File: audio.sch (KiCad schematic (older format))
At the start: 37 parts

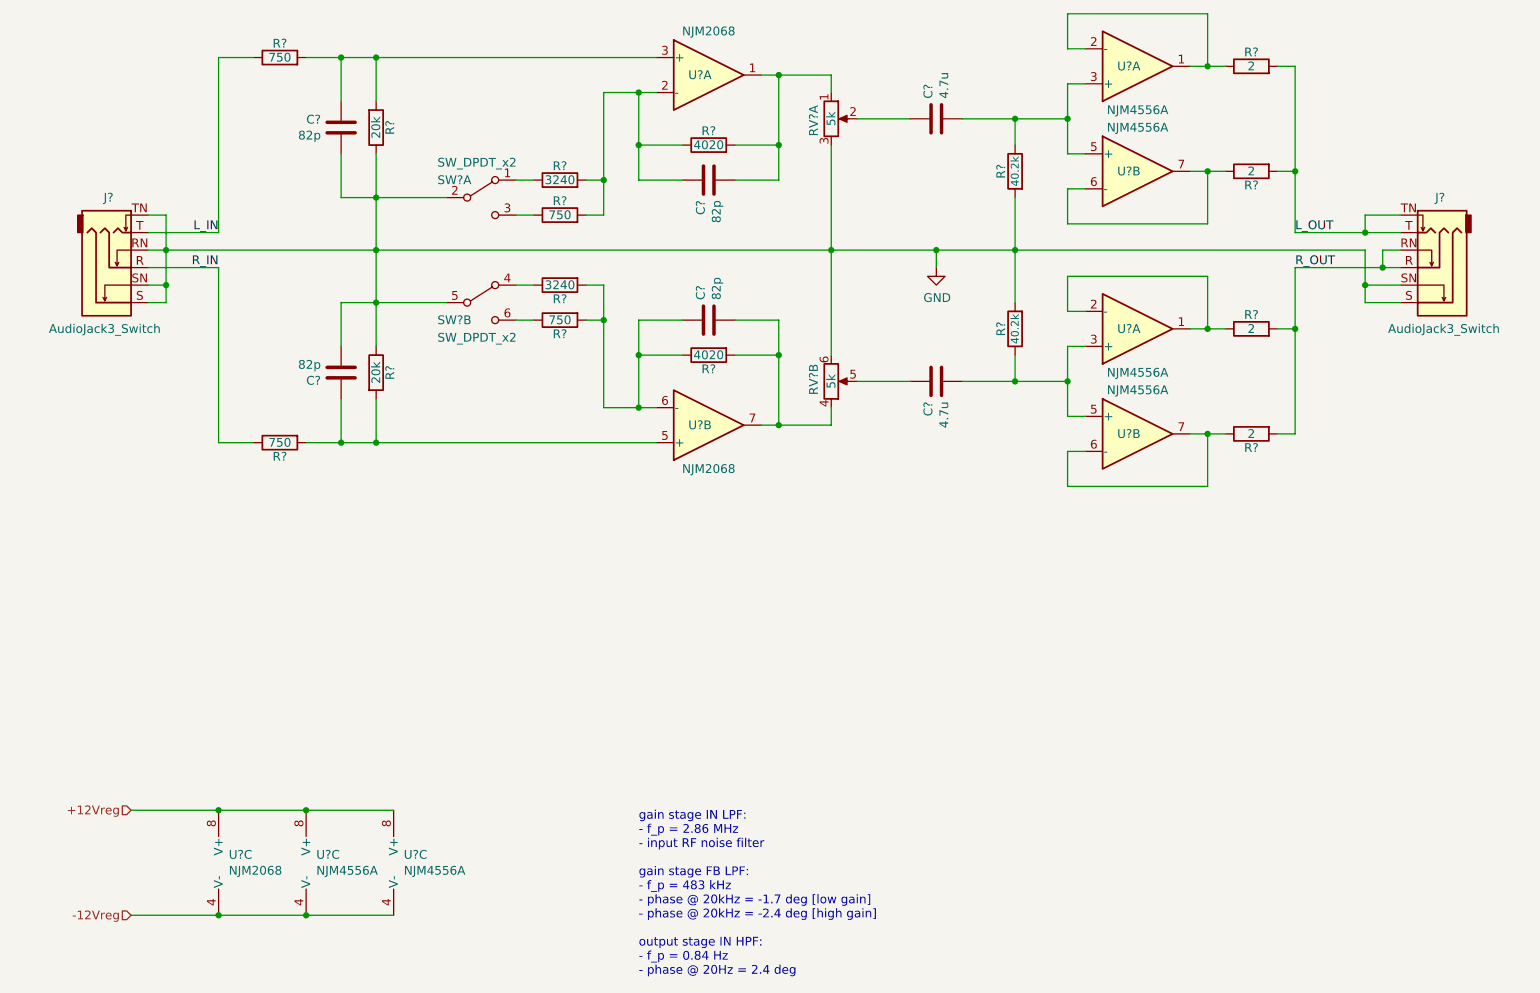
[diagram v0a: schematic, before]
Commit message: cleanup of wiring & notes in audio.sch
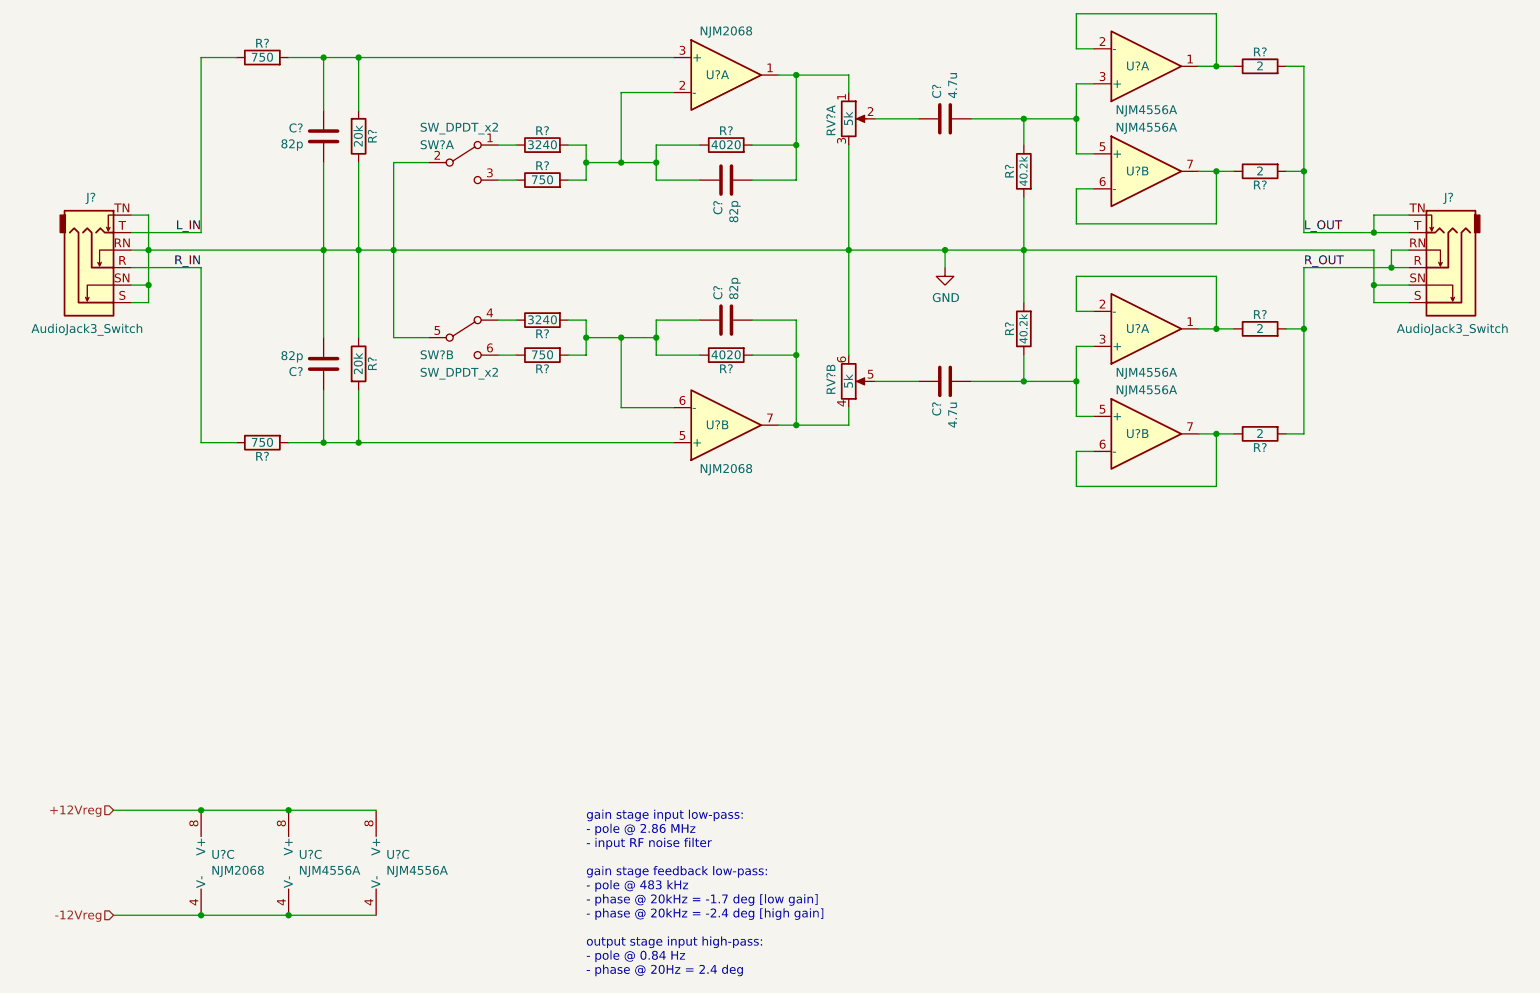
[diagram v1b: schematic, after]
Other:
- note added: "gain stage input low-pass:\n- pole @ 2.86 MHz\n- input RF noise filter\n\ngain stage feedback low-pass:\n- pole @ 483 kHz\n- phase @ 20kHz = -1.7 deg [low gain]\n- phase @ 20kHz = -2.4 deg [high gain]\n\noutput stage input high-pass:\n- pole @ 0.84 Hz\n- phase @ 20Hz = 2.4 deg"
- note removed: "gain stage IN LPF:\n- f_p = 2.86 MHz\n- input RF noise filter\n\ngain stage FB LPF:\n- f_p = 483 kHz\n- phase @ 20kHz = -1.7 deg [low gain]\n- phase @ 20kHz = -2.4 deg [high gain]\n\noutput stage IN HPF:\n- f_p = 0.84 Hz\n- phase @ 20Hz = 2.4 deg"
- moved on the sheet: C?, J?, R?, RV?A, RV?B, SW?A, SW?B, U?A, U?B, U?C

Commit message: add bourns SRU5028A inductor model & footprint
- switch location of bourns pot footprint
- update sourcing
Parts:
- RV?: footprint stdlibmods:Potentiometer_PTD902-1015K-A502 -> bourns:PTD902-1015K-A502
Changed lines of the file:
@@
 F 0 "RV?" V 6200 2550 50  0000 L CNN
 F 1 "5k" V 6300 2650 50  0000 C CNN
-F 2 "stdlibmods:Potentiometer_PTD902-1015K-A502" H 6300 2650 50  0001 C CNN
+F 2 "bourns:PTD902-1015K-A502" H 6300 2650 50  0001 C CNN
 F 3 "https://www.bourns.com/docs/product-datasheets/PTD90.pdf" H 6300 2650 50  0001 C CNN
 F 4 "Potentiometer 2 Gang Audio Taper 5kOhms" H 0   -600 50  0001 C CNN "Description"

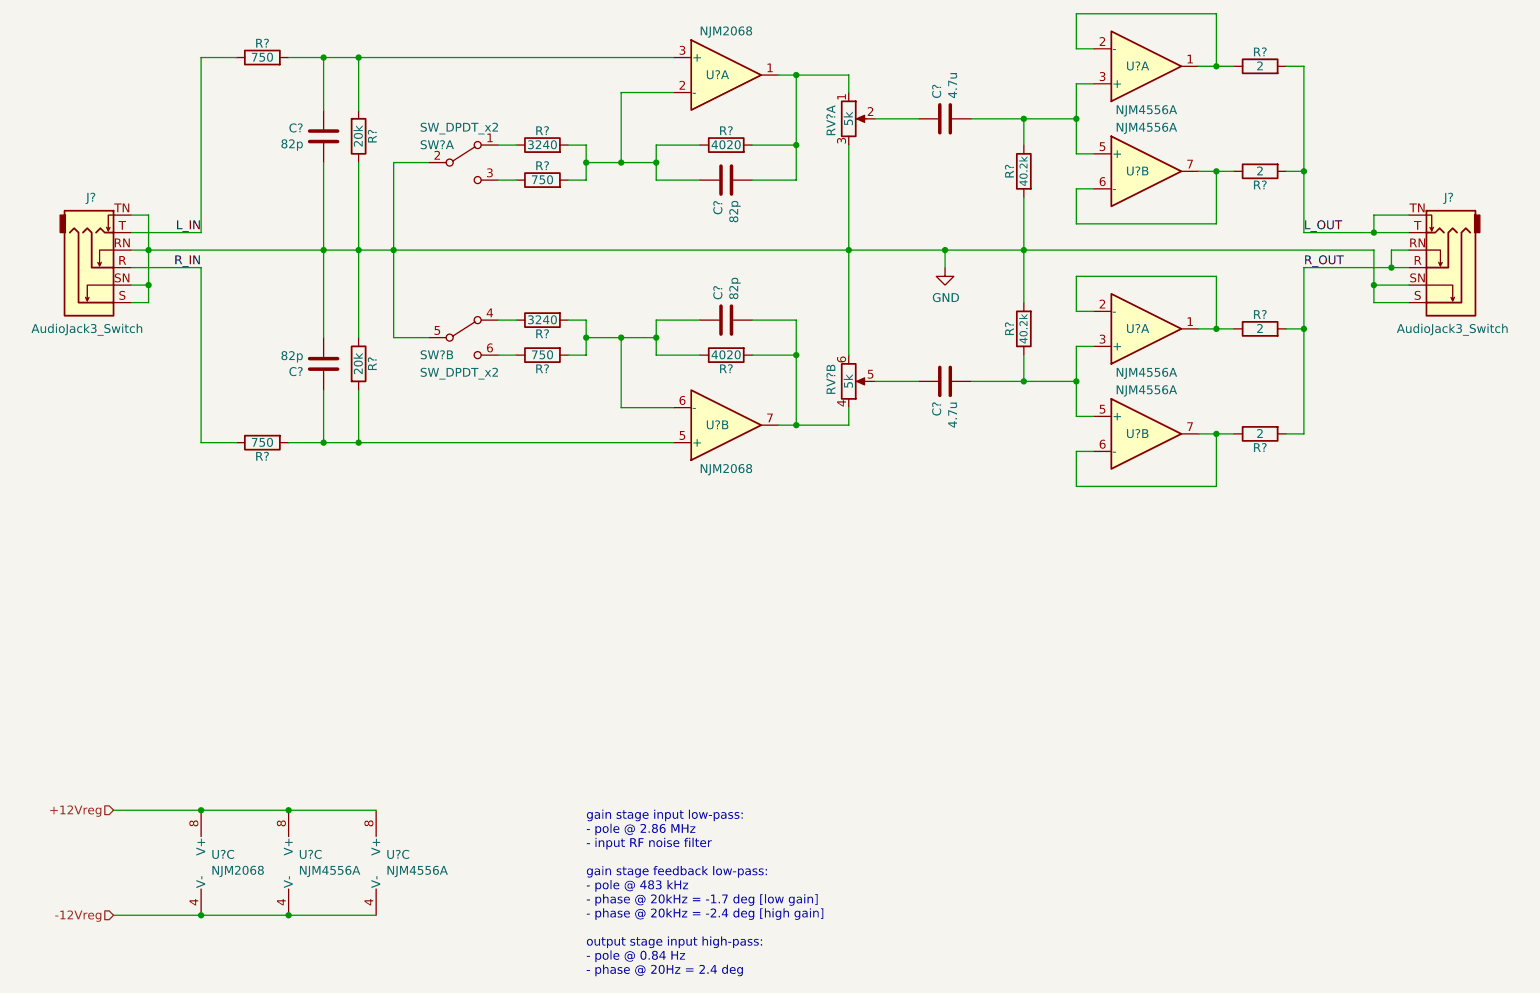
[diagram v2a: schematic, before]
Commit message: update output high pass filter
- replace WIMA 4.7uF coupling caps for KEMET 1uF
- replace 40.2k resistors with 274k
- update note
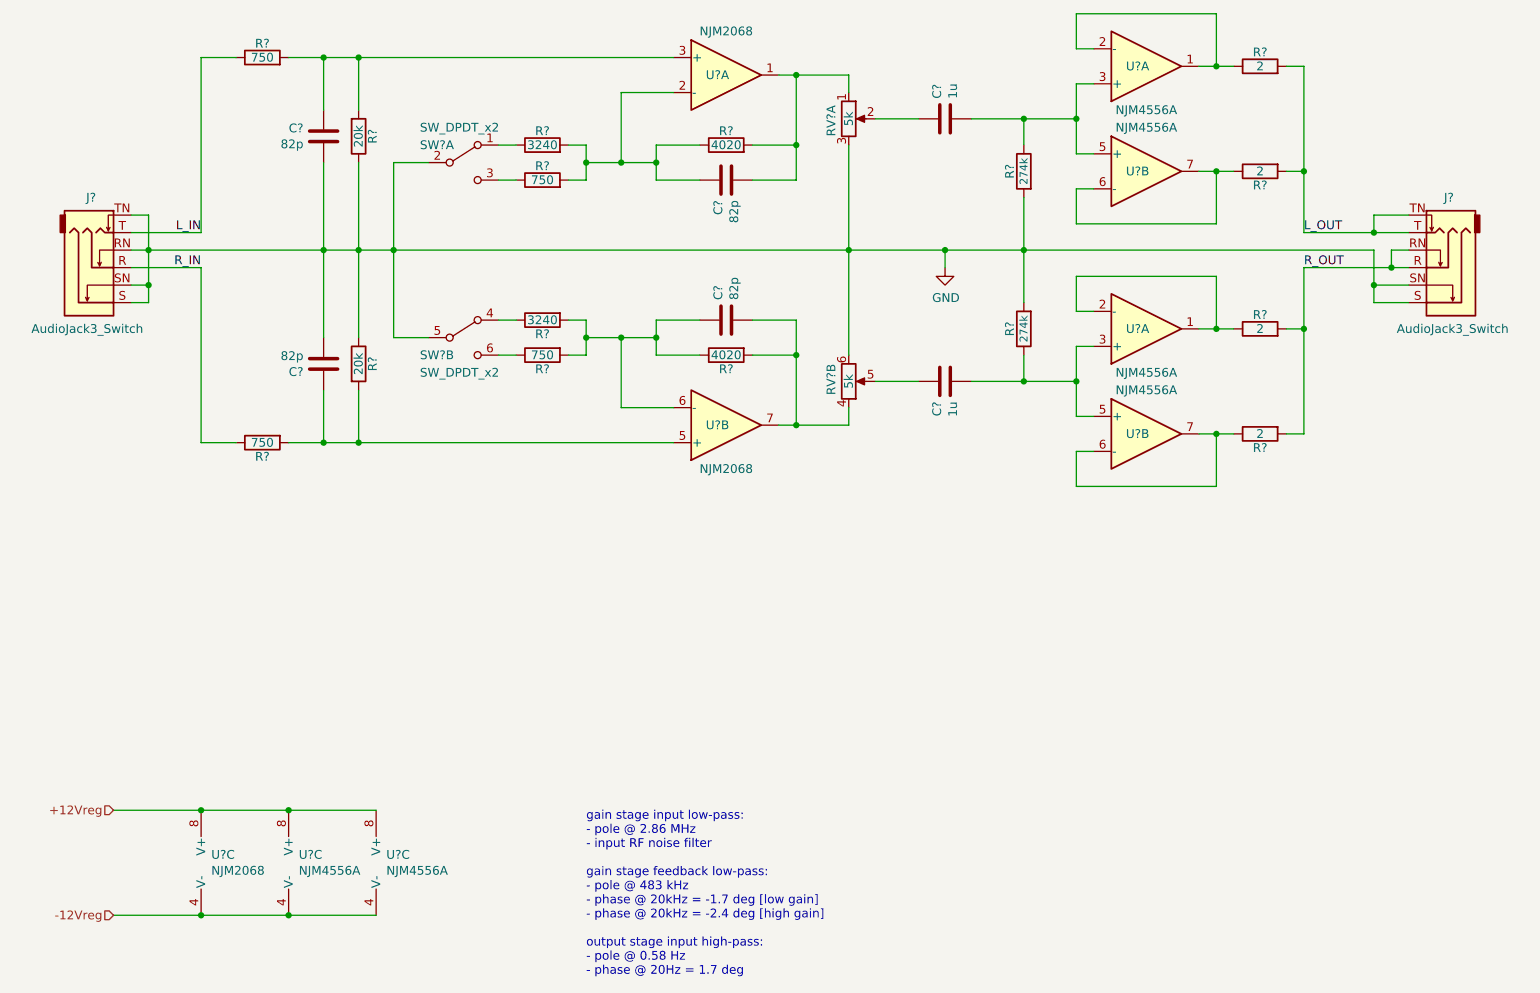
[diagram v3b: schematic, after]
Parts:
- C? (x2): value 4.7u -> 1u; footprint Capacitor_THT:C_Rect_L31.5mm_W15.0mm_P27.50mm_MKS4 -> (none); Description Film Capacitors 4.7uF 250 Volts 5% -> Film Capacitors 100V 1uF 5%; Manufacturer WIMA -> KEMET; Manufacturer Part Number MKP4F044706F00JSSD -> F612JT105J100R; Supplier Part Number 505-MKP4F044706F00JS -> 80-F612JT105J100R
- R? (x2): value 40.2k -> 274k; Description RES SMD 40.2K OHM 0.1% 1/8W 0805 Metal Film -> RES SMD 274K OHM 0.1% 1/8W 0805 Metal Film; Manufacturer Part Number ERA-6AEB4022V -> ERA-6AEB2743V; Supplier Part Number P40.2KDACT-ND -> P274KDACT-ND
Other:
- note added: "gain stage input low-pass:\n- pole @ 2.86 MHz\n- input RF noise filter\n\ngain stage feedback low-pass:\n- pole @ 483 kHz\n- phase @ 20kHz = -1.7 deg [low gain]\n- phase @ 20kHz = -2.4 deg [high gain]\n\noutput stage input high-pass:\n- pole @ 0.58 Hz\n- phase @ 20Hz = 1.7 deg"
- note removed: "gain stage input low-pass:\n- pole @ 2.86 MHz\n- input RF noise filter\n\ngain stage feedback low-pass:\n- pole @ 483 kHz\n- phase @ 20kHz = -1.7 deg [low gain]\n- phase @ 20kHz = -2.4 deg [high gain]\n\noutput stage input high-pass:\n- pole @ 0.84 Hz\n- phase @ 20Hz = 2.4 deg"
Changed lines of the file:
@@
 AR Path="/5CB56C16/5CEDA2A4" Ref="C?"  Part="1"
 F 0 "C?" H 6735 2604 50  0000 R CNN
-F 1 "4.7u" H 6735 2695 50  0000 R CNN
-F 2 "Capacitor_THT:C_Rect_L31.5mm_W15.0mm_P27.50mm_MKS4" H 6888 2500 50  0001 C CNN
-F 3 "https://www.mouser.com/datasheet/2/440/e_WIMA_MKP_4-1139861.pdf" H 6850 2650 50  0001 C CNN
-F 4 "Film Capacitors 4.7uF 250 Volts 5%" H 4400 -2500 50  0001 C CNN "Description"
-F 5 "WIMA" H 4400 -2500 50  0001 C CNN "Manufacturer"
-F 6 "MKP4F044706F00JSSD" H 4400 -2500 50  0001 C CNN "Manufacturer Part Number"
+F 1 "1u" H 6735 2695 50  0000 R CNN
+F 2 "" H 6888 2500 50  0001 C CNN
+F 3 "https://www.mouser.com/datasheet/2/212/KEM_F3065_F611_F612-1103659.pdf" H 6850 2650 50  0001 C CNN
+F 4 "Film Capacitors 100V 1uF 5%" H 4400 -2500 50  0001 C CNN "Description"
+F 5 "KEMET" H 4400 -2500 50  0001 C CNN "Manufacturer"
+F 6 "F612JT105J100R" H 4400 -2500 50  0001 C CNN "Manufacturer Part Number"
 F 7 "Mouser" H 4400 -2500 50  0001 C CNN "Supplier"
-F 8 "505-MKP4F044706F00JS" H 4400 -2500 50  0001 C CNN "Supplier Part Number"
+F 8 "80-F612JT105J100R" H 4400 -2500 50  0001 C CNN "Supplier Part Number"
 	1    6850 2650
 	0    1    1    0
@@
 AR Path="/5CB56C16/5CEDAB07" Ref="R?"  Part="1"
 F 0 "R?" V 7380 2950 50  0000 C CNN
-F 1 "40.2k" V 7300 2950 45  0000 C CNN
+F 1 "274k" V 7300 2950 45  0000 C CNN
 F 2 "Resistor_SMD:R_0805_2012Metric_Pad1.15x1.40mm_HandSolder" V 7230 2950 50  0001 C CNN
 F 3 "https://industrial.panasonic.com/cdbs/www-data/pdf/RDM0000/AOA0000C307.pdf" H 7300 2950 50  0001 C CNN
-F 4 "RES SMD 40.2K OHM 0.1% 1/8W 0805 Metal Film" H 7300 2950 50  0001 C CNN "Description"
+F 4 "RES SMD 274K OHM 0.1% 1/8W 0805 Metal Film" H 7300 2950 50  0001 C CNN "Description"
 F 5 "Panasonic Electronic Components" H 7300 2950 50  0001 C CNN "Manufacturer"
-F 6 "ERA-6AEB4022V" H 7300 2950 50  0001 C CNN "Manufacturer Part Number"
+F 6 "ERA-6AEB2743V" H 7300 2950 50  0001 C CNN "Manufacturer Part Number"
 F 7 "Digi-Key" H 7300 2950 50  0001 C CNN "Supplier"
-F 8 "P40.2KDACT-ND" H 7300 2950 50  0001 C CNN "Supplier Part Number"
+F 8 "P274KDACT-ND" H 7300 2950 50  0001 C CNN "Supplier Part Number"
 	1    7300 2950
 	-1   0    0    -1
@@
 AR Path="/5CB56C16/5CEE5E0B" Ref="C?"  Part="1"
 F 0 "C?" H 6735 4104 50  0000 R CNN
-F 1 "4.7u" H 6735 4195 50  0000 R CNN
-F 2 "Capacitor_THT:C_Rect_L31.5mm_W15.0mm_P27.50mm_MKS4" H 6888 4000 50  0001 C CNN
-F 3 "https://www.mouser.com/datasheet/2/440/e_WIMA_MKP_4-1139861.pdf" H 6850 4150 50  0001 C CNN
-F 4 "Film Capacitors 4.7uF 250 Volts 5%" H 4400 -1000 50  0001 C CNN "Description"
-F 5 "WIMA" H 4400 -1000 50  0001 C CNN "Manufacturer"
-F 6 "MKP4F044706F00JSSD" H 4400 -1000 50  0001 C CNN "Manufacturer Part Number"
+F 1 "1u" H 6735 4195 50  0000 R CNN
+F 2 "" H 6888 4000 50  0001 C CNN
+F 3 "https://www.mouser.com/datasheet/2/212/KEM_F3065_F611_F612-1103659.pdf" H 6850 4150 50  0001 C CNN
+F 4 "Film Capacitors 100V 1uF 5%" H 4400 -1000 50  0001 C CNN "Description"
+F 5 "KEMET" H 4400 -1000 50  0001 C CNN "Manufacturer"
+F 6 "F612JT105J100R" H 4400 -1000 50  0001 C CNN "Manufacturer Part Number"
 F 7 "Mouser" H 4400 -1000 50  0001 C CNN "Supplier"
-F 8 "505-MKP4F044706F00JS" H 4400 -1000 50  0001 C CNN "Supplier Part Number"
+F 8 "80-F612JT105J100R" H 4400 -1000 50  0001 C CNN "Supplier Part Number"
 	1    6850 4150
 	0    1    -1   0
@@
 AR Path="/5CB56C16/5CEE5E17" Ref="R?"  Part="1"
 F 0 "R?" V 7380 3850 50  0000 C CNN
-F 1 "40.2k" V 7300 3850 45  0000 C CNN
+F 1 "274k" V 7300 3850 45  0000 C CNN
 F 2 "Resistor_SMD:R_0805_2012Metric_Pad1.15x1.40mm_HandSolder" V 7230 3850 50  0001 C CNN
 F 3 "https://industrial.panasonic.com/cdbs/www-data/pdf/RDM0000/AOA0000C307.pdf" H 7300 3850 50  0001 C CNN
-F 4 "RES SMD 40.2K OHM 0.1% 1/8W 0805 Metal Film" H 7300 3850 50  0001 C CNN "Description"
+F 4 "RES SMD 274K OHM 0.1% 1/8W 0805 Metal Film" H 7300 3850 50  0001 C CNN "Description"
 F 5 "Panasonic Electronic Components" H 7300 3850 50  0001 C CNN "Manufacturer"
-F 6 "ERA-6AEB4022V" H 7300 3850 50  0001 C CNN "Manufacturer Part Number"
+F 6 "ERA-6AEB2743V" H 7300 3850 50  0001 C CNN "Manufacturer Part Number"
 F 7 "Digi-Key" H 7300 3850 50  0001 C CNN "Supplier"
-F 8 "P40.2KDACT-ND" H 7300 3850 50  0001 C CNN "Supplier Part Number"
+F 8 "P274KDACT-ND" H 7300 3850 50  0001 C CNN "Supplier Part Number"
 	1    7300 3850
 	-1   0    0    1
@@
 Connection ~ 9300 3600
 Text Notes 4800 7550 0    50   ~ 0
-gain stage input low-pass:\n- pole @ 2.86 MHz\n- input RF noise filter\n\ngain stage feedback low-pass:\n- pole @ 483 kHz\n- phase @ 20kHz = -1.7 deg [low gain]\n- phase @ 20kHz = -2.4 deg [high gain]\n\noutput stage input high-pass:\n- pole @ 0.84 Hz\n- phase @ 20Hz = 2.4 deg
+gain stage input low-pass:\n- pole @ 2.86 MHz\n- input RF noise filter\n\ngain stage feedback low-pass:\n- pole @ 483 kHz\n- phase @ 20kHz = -1.7 deg [low gain]\n- phase @ 20kHz = -2.4 deg [high gain]\n\noutput stage input high-pass:\n- pole @ 0.58 Hz\n- phase @ 20Hz = 1.7 deg
 Wire Wire Line
 	4800 2900 5000 2900

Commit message: update output stage coupled caps
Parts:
- C? (x2): Description Film Capacitors 100V 1uF 5% -> Film Capacitors 400V 1uF 2%; Manufacturer Part Number F612JT105J100R -> F461DP105G400L; Supplier Part Number 80-F612JT105J100R -> 80-F461DP105G400L
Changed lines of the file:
@@
 F 1 "1u" H 6735 2695 50  0000 R CNN
 F 2 "" H 6888 2500 50  0001 C CNN
-F 3 "https://www.mouser.com/datasheet/2/212/KEM_F3065_F611_F612-1103659.pdf" H 6850 2650 50  0001 C CNN
-F 4 "Film Capacitors 100V 1uF 5%" H 4400 -2500 50  0001 C CNN "Description"
+F 3 "https://www.mouser.com/datasheet/2/212/KEM_F3028_F461-464-1103031.pdf" H 6850 2650 50  0001 C CNN
+F 4 "Film Capacitors 400V 1uF 2%" H 4400 -2500 50  0001 C CNN "Description"
 F 5 "KEMET" H 4400 -2500 50  0001 C CNN "Manufacturer"
-F 6 "F612JT105J100R" H 4400 -2500 50  0001 C CNN "Manufacturer Part Number"
+F 6 "F461DP105G400L" H 4400 -2500 50  0001 C CNN "Manufacturer Part Number"
 F 7 "Mouser" H 4400 -2500 50  0001 C CNN "Supplier"
-F 8 "80-F612JT105J100R" H 4400 -2500 50  0001 C CNN "Supplier Part Number"
+F 8 "80-F461DP105G400L" H 4400 -2500 50  0001 C CNN "Supplier Part Number"
 	1    6850 2650
 	0    1    1    0
@@
 F 1 "1u" H 6735 4195 50  0000 R CNN
 F 2 "" H 6888 4000 50  0001 C CNN
-F 3 "https://www.mouser.com/datasheet/2/212/KEM_F3065_F611_F612-1103659.pdf" H 6850 4150 50  0001 C CNN
-F 4 "Film Capacitors 100V 1uF 5%" H 4400 -1000 50  0001 C CNN "Description"
+F 3 "https://www.mouser.com/datasheet/2/212/KEM_F3028_F461-464-1103031.pdf" H 6850 4150 50  0001 C CNN
+F 4 "Film Capacitors 400V 1uF 2%" H 4400 -1000 50  0001 C CNN "Description"
 F 5 "KEMET" H 4400 -1000 50  0001 C CNN "Manufacturer"
-F 6 "F612JT105J100R" H 4400 -1000 50  0001 C CNN "Manufacturer Part Number"
+F 6 "F461DP105G400L" H 4400 -1000 50  0001 C CNN "Manufacturer Part Number"
 F 7 "Mouser" H 4400 -1000 50  0001 C CNN "Supplier"
-F 8 "80-F612JT105J100R" H 4400 -1000 50  0001 C CNN "Supplier Part Number"
+F 8 "80-F461DP105G400L" H 4400 -1000 50  0001 C CNN "Supplier Part Number"
 	1    6850 4150
 	0    1    -1   0
